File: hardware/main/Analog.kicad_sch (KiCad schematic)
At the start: 60 parts, among them J301 Overvoltage_protection, J302 Rad_sensor, J303 Mos_temp, J304 Diode_temp, U301 INA823DT, U302 INA823DT, U303 INA293A4, U304 INA293A4, U305 TL7726IDR_1

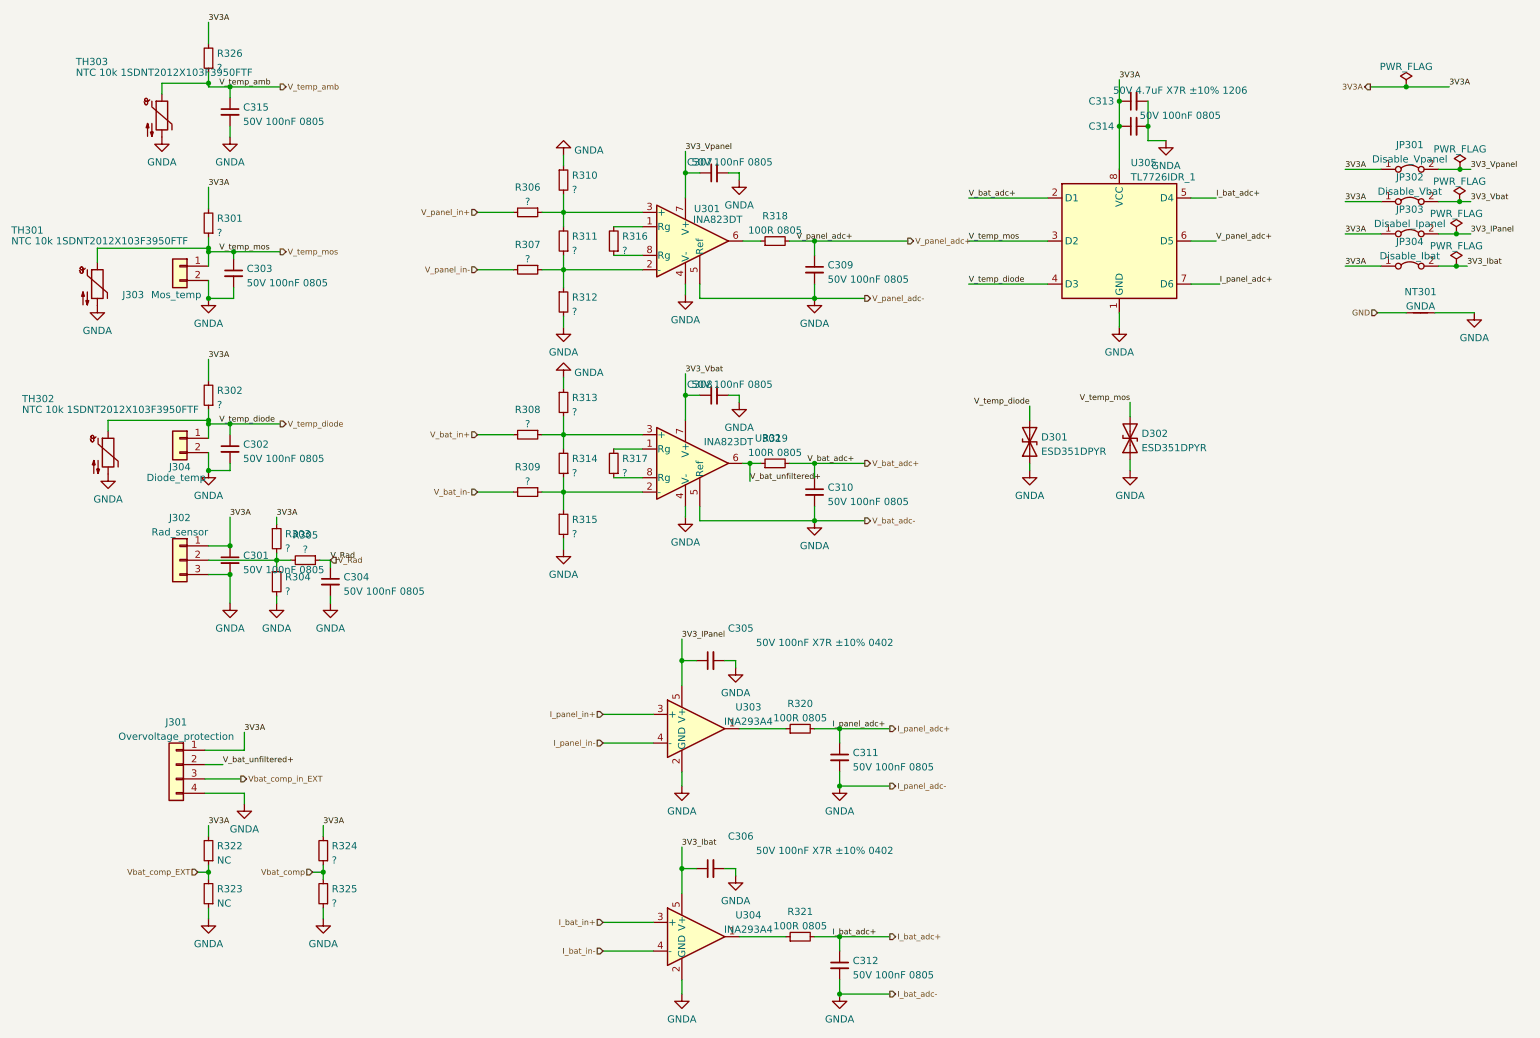
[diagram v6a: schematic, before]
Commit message: Layout: Finalize first vesion of control (DRC ok) and modify vias for better via density
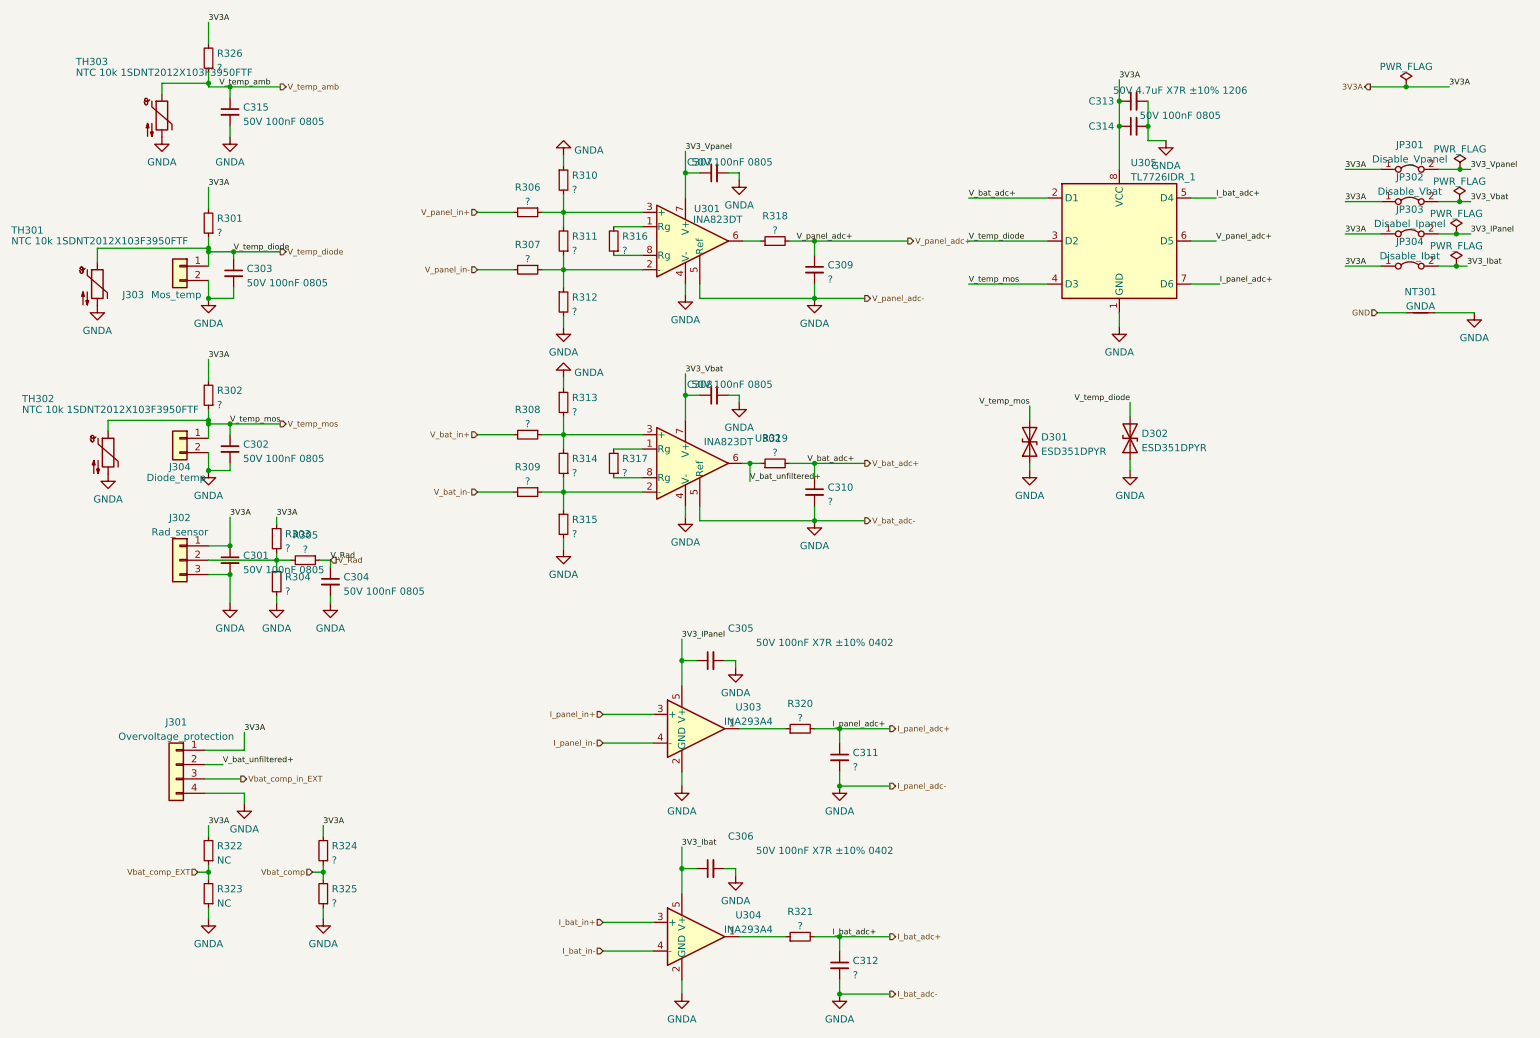
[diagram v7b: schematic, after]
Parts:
- C309, C310, C311, C312: value 50V 100nF 0805 -> ?
- NT301: footprint Resistor_SMD:R_0201_0603Metric -> Zenite:NetTie-2_SMD_Pad0.3mm
- R318, R319, R320, R321: value 100R 0805 -> ?
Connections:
- net V_temp_diode: now also C303.1, D302.2 (A2), J303.1 (Pin_1), R301.1, TH301.1, U305.3 (D2); no longer C302.1, D301.2 (A2), J304.1 (Pin_1), R302.1, TH302.1, U305.4 (D3)
- net V_temp_mos: now also C302.1, D301.2 (A2), J304.1 (Pin_1), R302.1, TH302.1, U305.4 (D3); no longer C303.1, D302.2 (A2), J303.1 (Pin_1), R301.1, TH301.1, U305.3 (D2)
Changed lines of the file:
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@@
     (effects (font (size 1.016 1.016)) (justify left bottom))
   )
-  (label "V_temp_mos" (at 46.355 55.245 0)
+  (label "V_temp_mos" (at 48.26 85.725 0)
     (effects (font (size 1.016 1.016)) (justify left bottom))
   )
@@
     (effects (font (size 1.016 1.016)) (justify left bottom))
   )
-  (label "V_temp_diode" (at 46.355 85.725 0)
+  (label "V_temp_diode" (at 48.895 55.245 0)
     (effects (font (size 1.016 1.016)) (justify left bottom))
   )
@@
     (effects (font (size 1.016 1.016)) (justify left bottom))
   )
-  (label "V_temp_mos" (at 207.645 81.915 180)
+  (label "V_temp_mos" (at 189.865 82.55 180)
     (effects (font (size 1.016 1.016)) (justify right bottom))
   )
@@
     (effects (font (size 1.016 1.016)) (justify left bottom))
   )
-  (label "V_temp_diode" (at 179.07 60.96 0)
+  (label "V_temp_diode" (at 179.07 53.34 0)
     (effects (font (size 1.016 1.016)) (justify left bottom))
   )
@@
     (effects (font (size 1.016 1.016)) (justify left bottom))
   )
-  (label "V_temp_diode" (at 189.865 82.55 180)
+  (label "V_temp_diode" (at 207.645 81.915 180)
     (effects (font (size 1.016 1.016)) (justify right bottom))
   )
@@
     (effects (font (size 1.016 1.016)) (justify left bottom))
   )
-  (label "V_temp_mos" (at 179.07 53.34 0)
+  (label "V_temp_mos" (at 179.07 60.96 0)
     (effects (font (size 1.016 1.016)) (justify left bottom))
   )
@@
     (effects (font (size 1.016 1.016)) (justify left))
   )
-  (hierarchical_label "V_temp_diode" (shape output) (at 57.15 85.725 0)
+  (hierarchical_label "V_temp_diode" (shape output) (at 57.15 55.245 0)
     (effects (font (size 1.016 1.016)) (justify left))
   )
@@
     (effects (font (size 1.016 1.016)) (justify right))
   )
-  (hierarchical_label "V_temp_mos" (shape output) (at 57.15 55.245 0)
+  (hierarchical_label "V_temp_mos" (shape output) (at 57.15 85.725 0)
     (effects (font (size 1.016 1.016)) (justify left))
   )
@@
       (effects (font (size 1.27 1.27)) (justify left))
     )
-    (property "Value" "50V 100nF 0805" (id 1) (at 154.0891 60.1285 0)
+    (property "Value" "?" (id 1) (at 154.0891 60.1285 0)
       (effects (font (size 1.27 1.27)) (justify left))
     )
@@
       (effects (font (size 1.27 1.27)) (justify left))
     )
-    (property "Value" "50V 100nF 0805" (id 1) (at 158.5341 183.3185 0)
+    (property "Value" "?" (id 1) (at 158.5341 183.3185 0)
       (effects (font (size 1.27 1.27)) (justify left))
     )
@@
       (effects (font (size 1.27 1.27)) (justify left))
     )
-    (property "Value" "50V 100nF 0805" (id 1) (at 154.0891 99.4985 0)
+    (property "Value" "?" (id 1) (at 154.0891 99.4985 0)
       (effects (font (size 1.27 1.27)) (justify left))
     )
@@
     (in_bom yes) (on_board yes) (fields_autoplaced)
     (property "Reference" "R320" (id 0) (at 149.225 135.2636 90))
-    (property "Value" "100R 0805" (id 1) (at 149.225 137.8005 90))
+    (property "Value" "?" (id 1) (at 149.225 137.8005 90))
     (property "Footprint" "Resistor_SMD:R_0805_2012Metric_Pad1.20x1.40mm_HandSolder" (id 2) (at 149.225 139.7 0)
       (effects (font (size 1.27 1.27)) hide)
@@
     (in_bom yes) (on_board yes) (fields_autoplaced)
     (property "Reference" "R318" (id 0) (at 144.78 48.9036 90))
-    (property "Value" "100R 0805" (id 1) (at 144.78 51.4405 90))
+    (property "Value" "?" (id 1) (at 144.78 51.4405 90))
     (property "Footprint" "Resistor_SMD:R_0805_2012Metric_Pad1.20x1.40mm_HandSolder" (id 2) (at 144.78 53.34 0)
       (effects (font (size 1.27 1.27)) hide)
@@
     (in_bom yes) (on_board yes) (fields_autoplaced)
     (property "Reference" "R321" (id 0) (at 149.225 172.0936 90))
-    (property "Value" "100R 0805" (id 1) (at 149.225 174.6305 90))
+    (property "Value" "?" (id 1) (at 149.225 174.6305 90))
     (property "Footprint" "Resistor_SMD:R_0805_2012Metric_Pad1.20x1.40mm_HandSolder" (id 2) (at 149.225 176.53 0)
       (effects (font (size 1.27 1.27)) hide)
@@
       (effects (font (size 1.27 1.27)) (justify left))
     )
-    (property "Value" "50V 100nF 0805" (id 1) (at 158.5341 146.4885 0)
+    (property "Value" "?" (id 1) (at 158.5341 146.4885 0)
       (effects (font (size 1.27 1.27)) (justify left))
     )
@@
     (in_bom yes) (on_board yes) (fields_autoplaced)
     (property "Reference" "R319" (id 0) (at 144.78 88.2736 90))
-    (property "Value" "100R 0805" (id 1) (at 144.78 90.8105 90))
+    (property "Value" "?" (id 1) (at 144.78 90.8105 90))
     (property "Footprint" "Resistor_SMD:R_0805_2012Metric_Pad1.20x1.40mm_HandSolder" (id 2) (at 144.78 92.71 0)
       (effects (font (size 1.27 1.27)) hide)
@@
     (property "Reference" "NT301" (id 0) (at 259.08 62.3402 0))
     (property "Value" "GNDA" (id 1) (at 259.08 64.8771 0))
-    (property "Footprint" "Resistor_SMD:R_0201_0603Metric" (id 2) (at 259.08 66.04 0)
-      (effects (font (size 1.27 1.27)) hide)
-    )
+    (property "Footprint" "Zenite:NetTie-2_SMD_Pad0.3mm" (id 2) (at 259.08 66.04 0)
+      (effects (font (size 1.27 1.27)) hide)
+    )

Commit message: Better GNDA + silk work
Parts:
- added NT302: GNDA, Zenite:NetTie-2_SMD_Pad0.3mm, symbol Device:NetTie_2
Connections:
- net GND: now also NT302.1
- net GNDA: now also NT302.2
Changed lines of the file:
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@@
+    (stroke (width 0) (type default) (color 0 0 0 0))
+  )
+  (wire (pts (xy 251.46 73.66) (xy 256.54 73.66))
     (stroke (width 0) (type default) (color 0 0 0 0))
   )
@@
   )
   (wire (pts (xy 156.21 139.7) (xy 156.21 142.24))
+    (stroke (width 0) (type default) (color 0 0 0 0))
+  )
+  (wire (pts (xy 261.62 73.66) (xy 268.605 73.66))
     (stroke (width 0) (type default) (color 0 0 0 0))
   )
@@
   )
   (hierarchical_label "3V3A" (shape output) (at 250.19 26.035 180)
+    (effects (font (size 1.016 1.016)) (justify right))
+  )
+  (hierarchical_label "GND" (shape input) (at 251.46 73.66 180)
     (effects (font (size 1.016 1.016)) (justify right))
   )
@@
     (pin "1")
   )
+  (symbol (lib_id "power:GNDA") (at 268.605 73.66 0) (unit 1)
+    (in_bom yes) (on_board yes) (fields_autoplaced)
+    (property "Reference" "#PWR01" (id 0) (at 268.605 80.01 0)
+      (effects (font (size 1.27 1.27)) hide)
+    )
+    (property "Value" "GNDA" (id 1) (at 268.605 78.1034 0))
+    (property "Footprint" "" (id 2) (at 268.605 73.66 0)
+      (effects (font (size 1.27 1.27)) hide)
+    )
+    (property "Datasheet" "" (id 3) (at 268.605 73.66 0)
+      (effects (font (size 1.27 1.27)) hide)
+    )
+    (pin "1")
+  )
   (symbol (lib_id "Device:C_Small") (at 151.765 97.79 0) (unit 1)
     (in_bom yes) (on_board yes) (fields_autoplaced)
@@
       (effects (font (size 1.27 1.27)) hide)
     )
+    (pin "1")
+    (pin "2")
+  )
+  (symbol (lib_id "Device:NetTie_2") (at 259.08 73.66 0) (unit 1)
+    (in_bom yes) (on_board yes) (fields_autoplaced)
+    (property "Reference" "NT302" (id 0) (at 259.08 68.58 0))
+    (property "Value" "GNDA" (id 1) (at 259.08 71.12 0))
+    (property "Footprint" "Zenite:NetTie-2_SMD_Pad0.3mm" (id 2) (at 259.08 73.66 0)
+      (effects (font (size 1.27 1.27)) hide)
+    )
+    (property "Datasheet" "~" (id 3) (at 259.08 73.66 0)
+      (effects (font (size 1.27 1.27)) hide)
+    )
